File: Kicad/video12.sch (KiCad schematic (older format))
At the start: 18 parts, among them J401 DE15HD, U401 THS7316, U402 TPD7S019

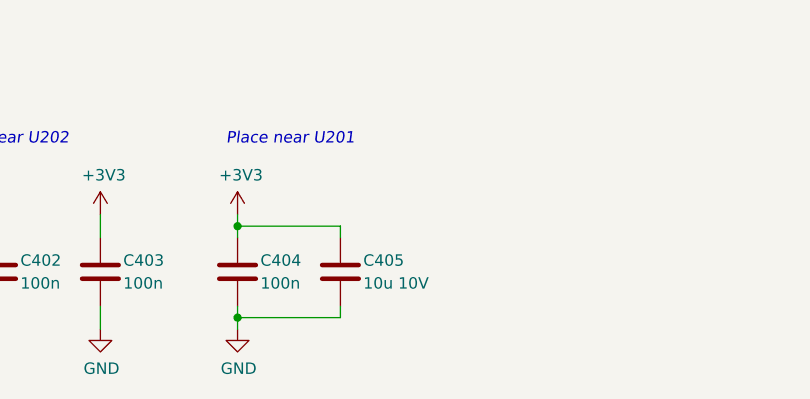
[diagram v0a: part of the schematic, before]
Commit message: Switching some parts over to the CPL.
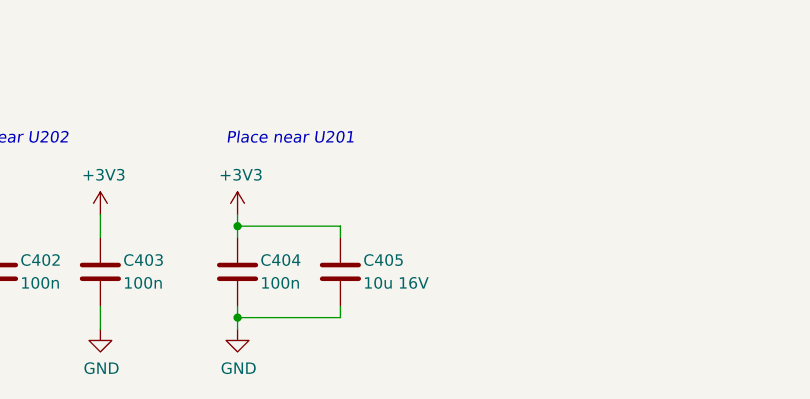
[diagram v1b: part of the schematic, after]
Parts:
- C401, C402, C403, C404: Digikey BC1150CT-ND -> (none); MPN K104K15X7RF5TL2 -> CPL-CAP-X7R-0805-100NF-50V; Manufacturer Vishay -> CPL; Mouser 594-K104K15X7RF5TL2 -> (none)
- C405: value 10u 10V -> 10u 16V; Digikey 1276-6455-1-ND -> (none); MPN CL21A106KOQNNNG -> CPL-CAP-X5R-0805-10UF-16V; Manufacturer Samsung -> CPL
- R401, R402, R403: Digikey RMCF0805FT10K0-ND -> (none); MPN RMCF0805FT10K0 -> CPL-RES-0805-10K-0.125W; Manufacturer Stackpole -> CPL
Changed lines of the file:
@@
 F 3 "~" H 3050 4150 50  0001 C CNN
 F 4 "0" H 3050 4150 50  0001 C CNN "DNP"
-F 5 "RMCF0805FT10K0-ND" H 3050 4150 50  0001 C CNN "Digikey"
-F 6 "RMCF0805FT10K0" H 3050 4150 50  0001 C CNN "MPN"
-F 7 "Stackpole" H 3050 4150 50  0001 C CNN "Manufacturer"
+F 5 "" H 3050 4150 50  0001 C CNN "Digikey"
+F 6 "CPL-RES-0805-10K-0.125W" H 3050 4150 50  0001 C CNN "MPN"
+F 7 "CPL" H 3050 4150 50  0001 C CNN "Manufacturer"
 	1    3050 4150
 	-1   0    0    1
@@
 F 3 "~" H 3500 4150 50  0001 C CNN
 F 4 "0" H 3500 4150 50  0001 C CNN "DNP"
-F 5 "RMCF0805FT10K0-ND" H 3500 4150 50  0001 C CNN "Digikey"
-F 6 "RMCF0805FT10K0" H 3500 4150 50  0001 C CNN "MPN"
-F 7 "Stackpole" H 3500 4150 50  0001 C CNN "Manufacturer"
+F 5 "" H 3500 4150 50  0001 C CNN "Digikey"
+F 6 "CPL-RES-0805-10K-0.125W" H 3500 4150 50  0001 C CNN "MPN"
+F 7 "CPL" H 3500 4150 50  0001 C CNN "Manufacturer"
 	1    3500 4150
 	-1   0    0    1
@@
 F 3 "~" H 3950 4150 50  0001 C CNN
 F 4 "0" H 3950 4150 50  0001 C CNN "DNP"
-F 5 "RMCF0805FT10K0-ND" H 3950 4150 50  0001 C CNN "Digikey"
-F 6 "RMCF0805FT10K0" H 3950 4150 50  0001 C CNN "MPN"
-F 7 "Stackpole" H 3950 4150 50  0001 C CNN "Manufacturer"
+F 5 "" H 3950 4150 50  0001 C CNN "Digikey"
+F 6 "CPL-RES-0805-10K-0.125W" H 3950 4150 50  0001 C CNN "MPN"
+F 7 "CPL" H 3950 4150 50  0001 C CNN "Manufacturer"
 	1    3950 4150
 	-1   0    0    1
@@
 F 3 "~" H 800 7150 50  0001 C CNN
 F 4 "0" H 800 7150 50  0001 C CNN "DNP"
-F 5 "BC1150CT-ND" H 800 7150 50  0001 C CNN "Digikey"
-F 6 "K104K15X7RF5TL2" H 800 7150 50  0001 C CNN "MPN"
-F 7 "Vishay" H 800 7150 50  0001 C CNN "Manufacturer"
-F 8 "594-K104K15X7RF5TL2" H 800 7150 50  0001 C CNN "Mouser"
+F 5 "" H 800 7150 50  0001 C CNN "Digikey"
+F 6 "CPL-CAP-X7R-0805-100NF-50V" H 800 7150 50  0001 C CNN "MPN"
+F 7 "CPL" H 800 7150 50  0001 C CNN "Manufacturer"
+F 8 "" H 800 7150 50  0001 C CNN "Mouser"
 	1    800  7150
 	-1   0    0    1
@@
 F 3 "~" H 1250 7150 50  0001 C CNN
 F 4 "0" H 1250 7150 50  0001 C CNN "DNP"
-F 5 "BC1150CT-ND" H 1250 7150 50  0001 C CNN "Digikey"
-F 6 "K104K15X7RF5TL2" H 1250 7150 50  0001 C CNN "MPN"
-F 7 "Vishay" H 1250 7150 50  0001 C CNN "Manufacturer"
-F 8 "594-K104K15X7RF5TL2" H 1250 7150 50  0001 C CNN "Mouser"
+F 5 "" H 1250 7150 50  0001 C CNN "Digikey"
+F 6 "CPL-CAP-X7R-0805-100NF-50V" H 1250 7150 50  0001 C CNN "MPN"
+F 7 "CPL" H 1250 7150 50  0001 C CNN "Manufacturer"
+F 8 "" H 1250 7150 50  0001 C CNN "Mouser"
 	1    1250 7150
 	-1   0    0    1
@@
 F 3 "~" H 2300 7150 50  0001 C CNN
 F 4 "0" H 2300 7150 50  0001 C CNN "DNP"
-F 5 "BC1150CT-ND" H 2300 7150 50  0001 C CNN "Digikey"
-F 6 "K104K15X7RF5TL2" H 2300 7150 50  0001 C CNN "MPN"
-F 7 "Vishay" H 2300 7150 50  0001 C CNN "Manufacturer"
-F 8 "594-K104K15X7RF5TL2" H 2300 7150 50  0001 C CNN "Mouser"
+F 5 "" H 2300 7150 50  0001 C CNN "Digikey"
+F 6 "CPL-CAP-X7R-0805-100NF-50V" H 2300 7150 50  0001 C CNN "MPN"
+F 7 "CPL" H 2300 7150 50  0001 C CNN "Manufacturer"
+F 8 "" H 2300 7150 50  0001 C CNN "Mouser"
 	1    2300 7150
 	-1   0    0    1
@@
 P 2750 7150
 F 0 "C405" H 2650 7200 50  0000 R CNN
-F 1 "10u 10V" H 2650 7100 50  0000 R CNN
+F 1 "10u 16V" H 2650 7100 50  0000 R CNN
 F 2 "Capacitor_SMD:C_0805_2012Metric_Pad1.18x1.45mm_HandSolder" H 2788 7000 50  0001 C CNN
 F 3 "~" H 2750 7150 50  0001 C CNN
 F 4 "0" H 2750 7150 50  0001 C CNN "DNP"
-F 5 "1276-6455-1-ND" H 2750 7150 50  0001 C CNN "Digikey"
-F 6 "CL21A106KOQNNNG" H 2750 7150 50  0001 C CNN "MPN"
-F 7 "Samsung" H 2750 7150 50  0001 C CNN "Manufacturer"
+F 5 "" H 2750 7150 50  0001 C CNN "Digikey"
+F 6 "CPL-CAP-X5R-0805-10UF-16V" H 2750 7150 50  0001 C CNN "MPN"
+F 7 "CPL" H 2750 7150 50  0001 C CNN "Manufacturer"
 	1    2750 7150
 	-1   0    0    -1
@@
 F 3 "~" H 1700 7150 50  0001 C CNN
 F 4 "0" H 1700 7150 50  0001 C CNN "DNP"
-F 5 "BC1150CT-ND" H 1700 7150 50  0001 C CNN "Digikey"
-F 6 "K104K15X7RF5TL2" H 1700 7150 50  0001 C CNN "MPN"
-F 7 "Vishay" H 1700 7150 50  0001 C CNN "Manufacturer"
-F 8 "594-K104K15X7RF5TL2" H 1700 7150 50  0001 C CNN "Mouser"
+F 5 "" H 1700 7150 50  0001 C CNN "Digikey"
+F 6 "CPL-CAP-X7R-0805-100NF-50V" H 1700 7150 50  0001 C CNN "MPN"
+F 7 "CPL" H 1700 7150 50  0001 C CNN "Manufacturer"
+F 8 "" H 1700 7150 50  0001 C CNN "Mouser"
 	1    1700 7150
 	-1   0    0    1

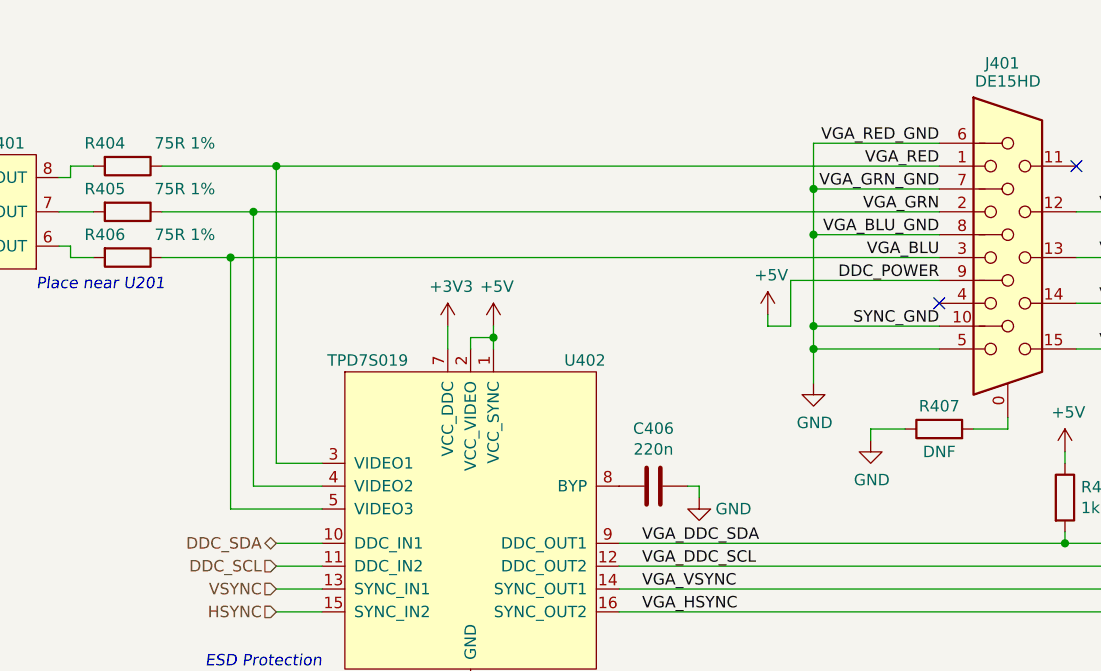
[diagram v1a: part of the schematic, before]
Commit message: Connnected up VGA DAC.
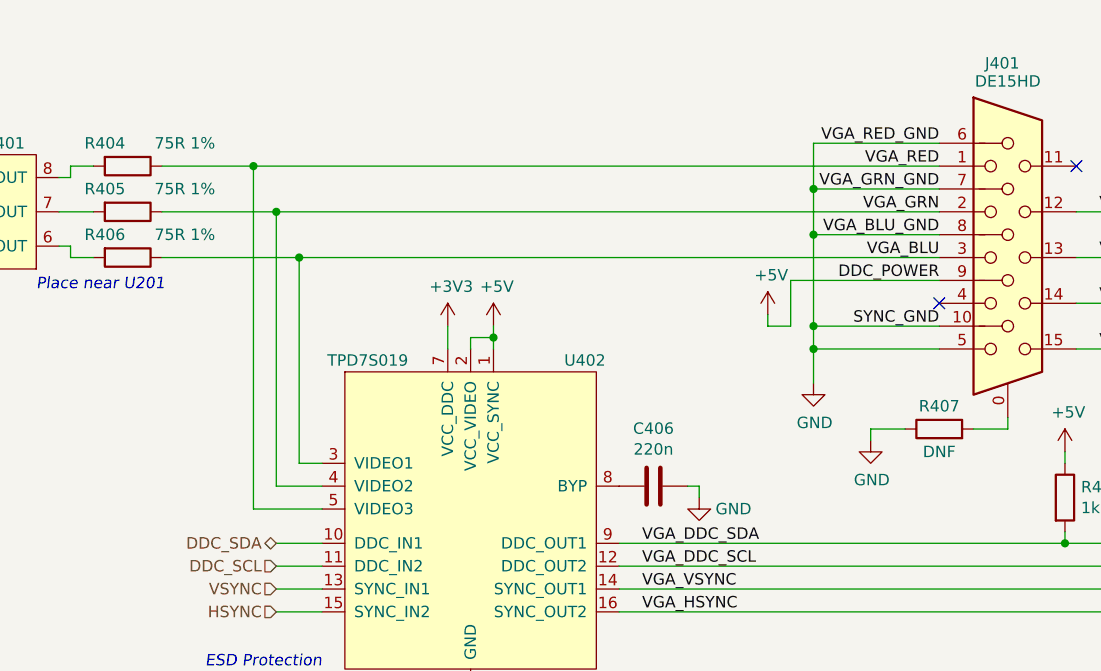
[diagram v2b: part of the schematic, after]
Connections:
- net VGA_BLU: now also U402.3 (VIDEO1); no longer U402.5 (VIDEO3)
- net VGA_RED: now also U402.5 (VIDEO3); no longer U402.3 (VIDEO1)
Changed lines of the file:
@@
 $Descr A4 11693 8268
 encoding utf-8
-Sheet 12 11
+Sheet 4 11
 Title ""
 Date "2021-04-17"
@@
 $EndComp
 Wire Wire Line
-	5650 3800 6050 3800
-Wire Wire Line
-	5650 4000 5950 4000
-Wire Wire Line
-	6350 4900 6150 4900
-Wire Wire Line
-	6150 3600 6150 4900
-Connection ~ 6150 3600
-Wire Wire Line
-	6050 5000 6350 5000
-Wire Wire Line
-	6350 5100 5950 5100
-Wire Wire Line
-	5950 5100 5950 4000
-Connection ~ 5950 4000
-Wire Wire Line
-	5650 3600 6150 3600
-Wire Wire Line
-	6050 3800 6050 5000
-Connection ~ 6050 3800
+	5650 3800 6150 3800
+Wire Wire Line
+	5650 4000 6250 4000
+Connection ~ 6050 3600
+Wire Wire Line
+	6150 5000 6350 5000
+Connection ~ 6250 4000
+Wire Wire Line
+	5650 3600 6050 3600
+Wire Wire Line
+	6150 3800 6150 5000
+Connection ~ 6150 3800
 $Comp
 L Neotron-Common-Hardware:TPF133A U401
@@
 	2300 6950 2300 6900
 Wire Wire Line
-	5950 4000 9050 4000
-Wire Wire Line
-	6050 3800 9050 3800
-Wire Wire Line
-	6150 3600 9050 3600
+	6250 4000 9050 4000
+Wire Wire Line
+	6150 3800 9050 3800
+Wire Wire Line
+	6050 3600 9050 3600
 $Comp
 L power:GND #PWR0413
@@
 Wire Wire Line
 	9600 5250 11050 5250
+Wire Wire Line
+	6350 5100 6050 5100
+Wire Wire Line
+	6050 3600 6050 5100
+Wire Wire Line
+	6350 4900 6250 4900
+Wire Wire Line
+	6250 4900 6250 4000
 $EndSCHEMATC

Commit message: Fixing some review comments.
* PCB has rounded corners.
* Add JLCPCB part numbers for SMT parts
* Fixed Fab layer
* Renumbered Slots
* Mounting holes do not have thermal relief

Closes #13 #12 and #10
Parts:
- C401, C402, C403, C404: LCSC Part# (none) -> C49678
- C405: LCSC Part# (none) -> C15850
- C406: LCSC Part# (none) -> C5378
- R401, R402, R403: LCSC Part# (none) -> C17414
- R404, R405, R406: LCSC Part# (none) -> C20638
- R408, R409: LCSC Part# (none) -> C4310
- U401: LCSC Part# (none) -> C155446
- U402: LCSC Part# (none) -> C337499
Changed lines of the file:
@@
 F 7 "Amphenol" H 9350 4000 50  0001 C CNN "Manufacturer"
 F 8 "649-ICD15S13E4GV00LF" H 9350 4000 50  0001 C CNN "Mouser"
+F 9 "~" H 9350 4000 50  0001 C CNN "LCSC Part#"
 	1    9350 4000
 	1    0    0    -1
@@
 F 6 "RMCF0805FT75R0" H 5500 3600 50  0001 C CNN "MPN"
 F 7 "Stackpole" H 5500 3600 50  0001 C CNN "Manufacturer"
+F 8 "C20638" H 5500 3600 50  0001 C CNN "LCSC Part#"
 	1    5500 3600
 	0    1    1    0
@@
 F 6 "RMCF0805FT75R0" H 5500 3800 50  0001 C CNN "MPN"
 F 7 "Stackpole" H 5500 3800 50  0001 C CNN "Manufacturer"
+F 8 "C20638" H 5500 3800 50  0001 C CNN "LCSC Part#"
 	1    5500 3800
 	0    1    1    0
@@
 F 6 "RMCF0805FT75R0" H 5500 4000 50  0001 C CNN "MPN"
 F 7 "Stackpole" H 5500 4000 50  0001 C CNN "Manufacturer"
+F 8 "C20638" H 5500 4000 50  0001 C CNN "LCSC Part#"
 	1    5500 4000
 	0    1    1    0
@@
 F 6 "CPL-RES-0805-10K-0.125W" H 3050 4150 50  0001 C CNN "MPN"
 F 7 "CPL" H 3050 4150 50  0001 C CNN "Manufacturer"
+F 8 "C17414" H 3050 4150 50  0001 C CNN "LCSC Part#"
 	1    3050 4150
 	-1   0    0    1
@@
 F 6 "CPL-RES-0805-10K-0.125W" H 3500 4150 50  0001 C CNN "MPN"
 F 7 "CPL" H 3500 4150 50  0001 C CNN "Manufacturer"
+F 8 "C17414" H 3500 4150 50  0001 C CNN "LCSC Part#"
 	1    3500 4150
 	-1   0    0    1
@@
 F 6 "CPL-RES-0805-10K-0.125W" H 3950 4150 50  0001 C CNN "MPN"
 F 7 "CPL" H 3950 4150 50  0001 C CNN "Manufacturer"
+F 8 "C17414" H 3950 4150 50  0001 C CNN "LCSC Part#"
 	1    3950 4150
 	-1   0    0    1
@@
 F 7 "296-27595-1-ND" H 7000 5100 50  0001 C CNN "Digikey"
 F 8 "595-TPD7S019-15DBQR" H 7000 5100 50  0001 C CNN "Mouser"
+F 9 "C337499" H 7000 5100 50  0001 C CNN "LCSC Part#"
 	1    7000 5100
 	1    0    0    -1
@@
 F 7 "THS7316" H 4750 3800 50  0001 C CNN "MPN"
 F 8 "595-THS7316DR" H 4750 3800 50  0001 C CNN "Mouser"
+F 9 "C155446" H 4750 3800 50  0001 C CNN "LCSC Part#"
 	1    4750 3800
 	1    0    0    -1
@@
 F 6 "RMCF0805FT1K50" H 9600 5050 50  0001 C CNN "MPN"
 F 7 "Stackpole" H 9600 5050 50  0001 C CNN "Manufacturer"
+F 8 "C4310" H 9600 5050 50  0001 C CNN "LCSC Part#"
 	1    9600 5050
 	1    0    0    -1
@@
 F 6 "RMCF0805FT1K50" H 10050 5050 50  0001 C CNN "MPN"
 F 7 "Stackpole" H 10050 5050 50  0001 C CNN "Manufacturer"
+F 8 "C4310" H 10050 5050 50  0001 C CNN "LCSC Part#"
 	1    10050 5050
 	1    0    0    -1
@@
 F 6 "CL21B224KBFNNNE" H 7800 5000 50  0001 C CNN "MPN"
 F 7 "Samsung" H 7800 5000 50  0001 C CNN "Manufacturer"
+F 8 "C5378" H 7800 5000 50  0001 C CNN "LCSC Part#"
 	1    7800 5000
 	0    1    1    0
@@
 F 7 "CPL" H 800 7150 50  0001 C CNN "Manufacturer"
 F 8 "" H 800 7150 50  0001 C CNN "Mouser"
+F 9 "C49678" H 800 7150 50  0001 C CNN "LCSC Part#"
 	1    800  7150
 	-1   0    0    1
@@
 F 7 "CPL" H 1250 7150 50  0001 C CNN "Manufacturer"
 F 8 "" H 1250 7150 50  0001 C CNN "Mouser"
+F 9 "C49678" H 1250 7150 50  0001 C CNN "LCSC Part#"
 	1    1250 7150
 	-1   0    0    1
@@
 F 7 "CPL" H 2300 7150 50  0001 C CNN "Manufacturer"
 F 8 "" H 2300 7150 50  0001 C CNN "Mouser"
+F 9 "C49678" H 2300 7150 50  0001 C CNN "LCSC Part#"
 	1    2300 7150
 	-1   0    0    1
@@
 F 6 "CPL-CAP-X5R-0805-10UF-16V" H 2750 7150 50  0001 C CNN "MPN"
 F 7 "CPL" H 2750 7150 50  0001 C CNN "Manufacturer"
+F 8 "C15850" H 2750 7150 50  0001 C CNN "LCSC Part#"
 	1    2750 7150
 	-1   0    0    -1
@@
 F 7 "~" H 9050 4750 50  0001 C CNN "Manufacturer"
 F 8 "" H 9050 4750 50  0001 C CNN "Mouser"
+F 9 "~" H 9050 4750 50  0001 C CNN "LCSC Part#"
 	1    9050 4750
 	0    -1   -1   0
@@
 F 7 "CPL" H 1700 7150 50  0001 C CNN "Manufacturer"
 F 8 "" H 1700 7150 50  0001 C CNN "Mouser"
+F 9 "C49678" H 1700 7150 50  0001 C CNN "LCSC Part#"
 	1    1700 7150
 	-1   0    0    1
